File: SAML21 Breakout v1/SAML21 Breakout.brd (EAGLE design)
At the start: 100 x 80 mm, 32 parts, among them J1 M50-4910545, U1 AT-SAM-L21-JTQFP, U2 AP7361C-33E-13, U3 MCP1501-CHY, Y2 32.768MHz

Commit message: dd
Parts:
- moved R3 3.59 mm to (38.1, 17.8), turned to 270 degrees
- moved D2 2.54 mm to (20.3, 17.8), turned to 90 degrees
- moved J1 2.54 mm to (55.9, 66.0)
- moved VREF_EN 2.54 mm to (33.0, 48.3)
- moved C14 1.91 mm to (36.2, 52.1)
- moved U3 1.90 mm to (37.5, 54.6)
- moved R5 1.80 mm to (22.9, 17.8), turned to 270 degrees
- moved D1 1.80 mm to (40.6, 17.8), turned to 90 degrees
- moved R4 1.27 mm to (36.8, 49.5)

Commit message: breakout
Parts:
- added JP1: M142ROWS, dr-library:2X07
- added JP2, JP3, JP8: M122ROWS, dr-library:2X06
- added JP4, JP5, JP6, JP7, JP9: M02LONG, dr-library:1X02-LONG
- moved J1 18.9 mm to (68.6, 52.1)
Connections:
- new net PA0: JP1.1, U1.1
- new net PA1: JP1.2, U1.2
- new net PA10: JP2.3, U1.19
- new net PA11: JP2.4, U1.20
- new net PA12: JP2.11, U1.29
- new net PA13: JP2.12, U1.30
- new net PA16: JP8.1, U1.35
- new net PA17: JP8.2, U1.36
- new net PA18: JP8.3, U1.37
- new net PA19: JP8.4, U1.38
- new net PA2: JP1.3, U1.3
- new net PA20: JP8.7, U1.41
- new net PA21: JP8.8, U1.42
- new net PA22: JP8.9, U1.43
- new net PA23: JP8.10, U1.44
- new net PA24: JP8.11, U1.45
- new net PA25: JP8.12, U1.46
- new net PA27: JP3.3, U1.51
- new net PA4: JP1.11, U1.13
- new net PA5: JP1.12, U1.14
- new net PA6: JP1.13, U1.15
- new net PA7: JP1.14, U1.16
- new net PA8: JP2.1, U1.17
- new net PA9: JP2.2, U1.18
- new net PB0: JP3.9, U1.61
- new net PB1: JP3.10, U1.62
- new net PB10: JP2.5, U1.23
- new net PB11: JP2.6, U1.24
- new net PB12: JP2.7, U1.25
- new net PB13: JP2.8, U1.26
- new net PB14: JP2.9, U1.27
- new net PB15: JP2.10, U1.28
- new net PB16: JP8.5, U1.39
- new net PB17: JP8.6, U1.40
- new net PB2: JP3.11, U1.63
- new net PB22: JP3.1, U1.49
- new net PB23: JP3.2, U1.50
- new net PB3: JP3.12, U1.64
- new net PB30: JP3.7, U1.59
- new net PB31: JP3.8, U1.60
- new net PB4: JP1.5, U1.5
- new net PB5: JP1.6, U1.6
- new net PB6: JP1.7, U1.9
- new net PB7: JP1.8, U1.10
- new net PB8: JP1.9, U1.11
- new net PB9: JP1.10, U1.12
- new net VSW: U1.55
- net +3V3: now also JP5.2, JP6.2, JP7.2, JP9.2
- net GND: now also JP4.2, JP5.1, JP6.1, JP7.1, JP9.1
- net RESET: now also JP3.4
- net SWCLK: now also JP3.5
- net SWDIO: now also JP3.6
- net VCC: now also JP4.1
- net VREF/PA3: now also JP1.4

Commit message: ddx
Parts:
- added D3, D4: PWR, dr-library:LED-1206
- added JP10, JP11: M02, dr-library:1X02
- added Q1, Q2: 2N7002, dr-library:SOT-23-3
- added R6, R8: 330, dr-library:RES-0603
- added R7, R9: 10k, dr-library:RES-0603
- added U$2, U$3, U$4, U$5: (no value), EmbeddedAdventures 3:STAND-OFF-HOLE
- moved JP4 80.3 mm to (94.0, 11.4), turned to 180 degrees
- moved D2 73.7 mm to (94.0, 17.8), turned to 180 degrees
- moved R5 71.2 mm to (94.0, 20.3), turned to 0 degrees
- moved C12 68.2 mm to (94.0, 23.5), turned to 180 degrees
- moved U2 64.3 mm to (94.0, 27.9), turned to 90 degrees
- moved C13 60.8 mm to (94.0, 32.4), turned to 180 degrees
- moved R3 58.6 mm to (94.0, 35.6), turned to 0 degrees
- moved D1 57.1 mm to (94.0, 38.1), turned to 180 degrees
- moved JP5 55.1 mm to (94.0, 41.9), turned to 0 degrees
- moved JP2 39.0 mm to (16.5, 11.4)
- moved JP6 37.8 mm to (11.4, 10.2)
- moved JP3 25.4 mm to (39.4, 59.7)
- moved JP7 25.4 mm to (22.9, 61.0)
- moved C3 19.2 mm to (36.8, 48.9)
- moved C5 19.2 mm to (46.4, 34.3)
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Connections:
- new net HEART: JP10.2, Q1.D, R7.1
- new net HEART2: JP11.2, Q2.D, R9.1
- new net N$10: D4.A, R8.1
- new net N$11: D4.C, Q2.G
- new net N$8: D3.A, R6.1
- new net N$9: D3.C, Q1.G
- net +3V3: now also R6.2, R8.2
- net GND: now also Q1.S, Q2.S, R7.2, R9.2
- net PA8: now also JP10.1
- net PB10: now also JP11.1
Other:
- board size 100 x 80 mm -> 76.2 x 63.5 mm

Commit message: component layout
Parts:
- added D5: VS-10BQ030-M3, dr-library:DO-214AA
- added J2: (no value), EmbeddedAdventures 3:SPC4077
- moved JP5 56.8 mm to (50.8, 5.08), turned to 90 degrees
- moved J1 54.6 mm to (7.62, 50.8)
- moved C12 52.6 mm to (46.4, 45.7), turned to 0 degrees
- moved U2 49.5 mm to (46.4, 41.3), turned to 270 degrees
- moved C13 47.8 mm to (46.4, 36.8), turned to 0 degrees
- moved S1 46.7 mm to (36.8, 58.4), turned to 180 degrees
- moved R2 43.5 mm to (43.2, 58.4), turned to 270 degrees
- moved R5 43.0 mm to (53.3, 34.3), turned to 180 degrees
- moved R8 41.6 mm to (53.3, 26.7), turned to 180 degrees
- moved R3 40.8 mm to (53.3, 31.8), turned to 180 degrees
- moved C9 39.8 mm to (36.8, 54.6), turned to 0 degrees
- moved D2 39.2 mm to (58.4, 34.3), turned to 0 degrees
- moved JP11 38.6 mm to (45.7, 31.8)
- moved R9 37.7 mm to (54.0, 21.6)
- moved JP10 37.4 mm to (45.7, 26.7)
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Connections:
- new net N$12: D5.A, J2.3
- net +3V3: no longer JP9.2
- net GND: now also J2.2, JP9.2; no longer JP9.1
- net VCC: now also D5.C, JP9.1
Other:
- board size 76.2 x 63.5 mm -> 63.5 x 63.5 mm

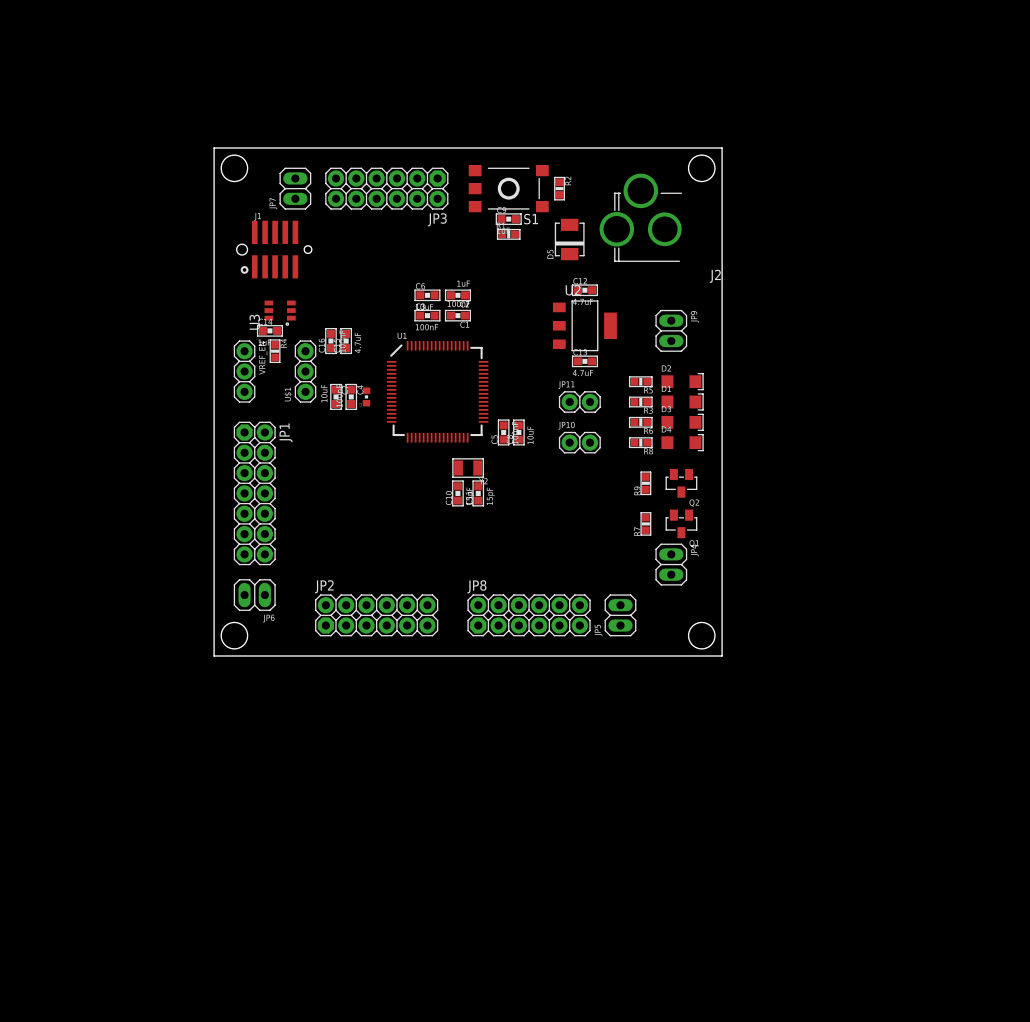
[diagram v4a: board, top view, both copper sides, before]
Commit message: Added USB interface
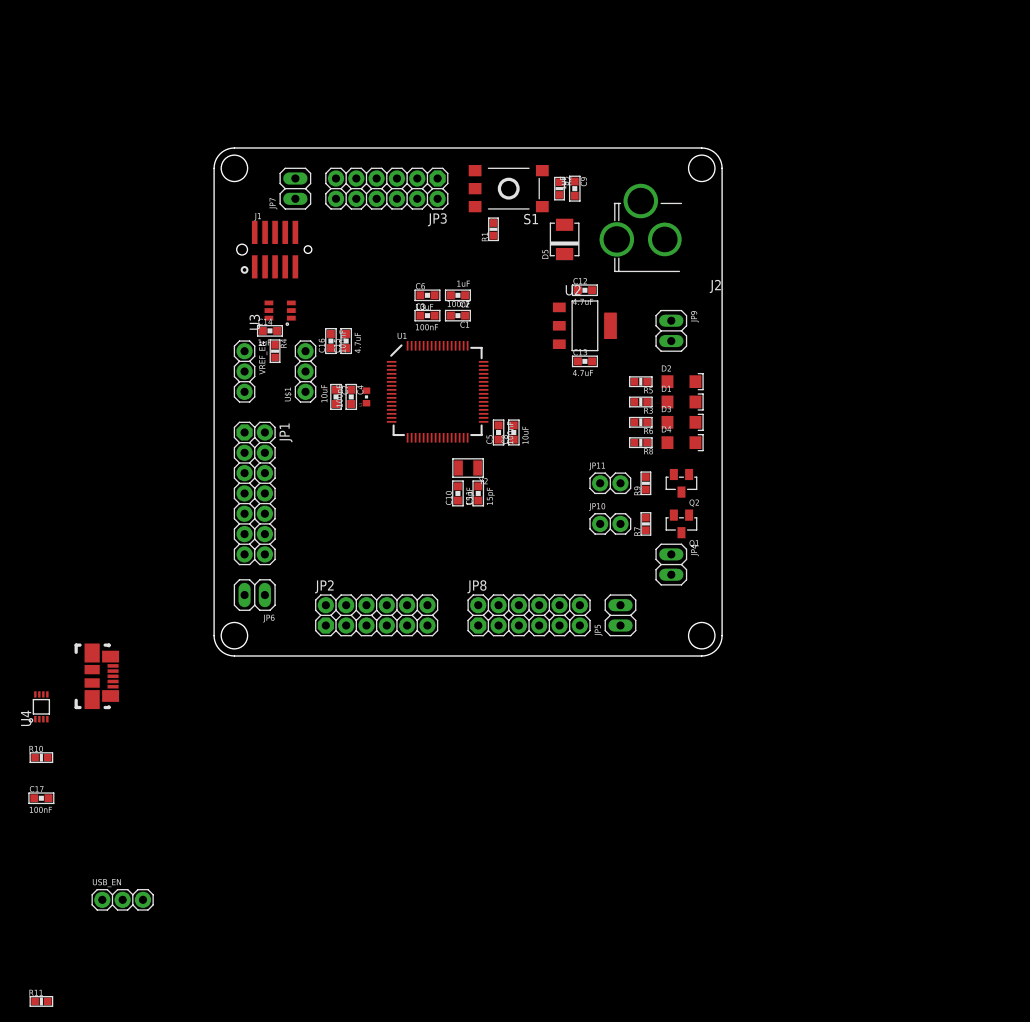
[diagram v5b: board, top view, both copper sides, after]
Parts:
- added C17: 100nF, dr-library:CAP-0603
- added R10, R11: 10k, dr-library:RES-0603
- added U$6: MOLEX_USBMICRO, dr-library:MOLEX_47346-001
- added U4: TXS-0102-Q1, dr-library:VSSOP-8
- added USB_EN: M03, dr-library:1X03
- moved JP10 10.9 mm to (49.5, 16.5)
- moved JP11 10.9 mm to (49.5, 21.6)
- moved C9 9.09 mm to (45.1, 58.4), turned to 270 degrees
- moved R1 2.01 mm to (34.9, 53.3), turned to 90 degrees
- moved J2 1.27 mm to (53.3, 52.1)
- moved D5 0.64 mm to (43.8, 52.1)
- moved C5 0.63 mm to (35.6, 27.9)
- moved C8 0.63 mm to (37.5, 27.9)
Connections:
- removed net PA24: JP8.11, U1.45
- removed net PA25: JP8.12, U1.46
- new net N$13: R10.1, USB_EN.1
- new net N$14: U$6.2, U4.8
- new net N$15: U$6.3, U4.1
- new net N$17: R11.2, USB_EN.3
- new net N$19: U4.6, USB_EN.2
- new net PA24/D-: JP8.11, U1.45, U4.5
- new net PA25/D+: JP8.12, U1.46, U4.4
- net +3V3: now also R10.2, U4.3
- net GND: now also C17.2, R11.1, U$6.5, U4.2
- net VCC: now also C17.1, U$6.1, U4.7
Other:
- outline, holes or cut-outs redrawn

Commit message: pcb layout
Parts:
- removed U2: AP7361C-33E-13, dr-library:SOT-223-3
- added U5: AP7362-33SP-13, dr-library:SO-8EP
- C12, C13: value 4.7uF -> 10uF
- moved R11 105.0 mm to (38.1, 43.2)
- moved C17 101.0 mm to (55.9, 47.0), turned to 270 degrees
- moved USB_EN 93.7 mm to (41.9, 45.7), turned to 180 degrees
- moved U$6 93.0 mm to (61.0, 50.8), turned to 180 degrees
- moved U4 87.1 mm to (48.3, 45.7), turned to 270 degrees
- moved R10 85.5 mm to (43.2, 43.2)
- moved C13 18.3 mm to (41.9, 54.6), turned to 270 degrees
- moved R4 12.9 mm to (3.17, 50.2)
- moved C9 12.7 mm to (45.1, 71.1)
- moved R1 12.7 mm to (34.9, 66.0), turned to 270 degrees
- moved R2 12.7 mm to (43.2, 71.1)
- moved S1 12.7 mm to (36.8, 71.1)
- moved D5 12.7 mm to (43.8, 64.8)
- moved J2 12.7 mm to (53.3, 64.8)
- moved U$3 12.7 mm to (2.54, 73.7)
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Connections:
- net +3V3: now also U5.5, U5.6, U5.7; no longer U2.3
- net GND: now also U5.1, U5.PAD; no longer U2.2
- net PA3: now also JP1.4
- net VCC: now also U5.2, U5.3, U5.4; no longer U2.1
- net VREF/PA3: no longer JP1.4
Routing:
- net +3V3: track 0.00 -> 359.7 mm, vias 0 -> 12
- net GND: track 0.00 -> 144.6 mm, vias 0 -> 9
- net VCC: track 0.00 -> 86.7 mm, vias 0 -> 2
- net RESET: track 0.00 -> 80.0 mm, vias 0 -> 2
- net PA8: track 0.00 -> 78.9 mm
- net PB10: track 0.00 -> 76.2 mm
- net PA24/D-: track 0.00 -> 58.5 mm, vias 0 -> 1
- net SWCLK: track 0.00 -> 57.6 mm, vias 0 -> 1
- net PA25/D+: track 0.00 -> 51.6 mm, vias 0 -> 1
- net SWDIO: track 0.00 -> 51.5 mm, vias 0 -> 1
- net PA22: track 0.00 -> 43.9 mm
- net PA20: track 0.00 -> 42.0 mm
- net PA23: track 0.00 -> 41.7 mm
- net PB16: track 0.00 -> 40.1 mm
- net PA21: track 0.00 -> 39.8 mm
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- added copper zone on layer 1, net +3V3
- added copper zone on layer 16, net +3V3
- added copper zone on layer 1, net GND
- added copper zone on layer 16, net GND
- added copper zone on layer 1, net N$3
- added copper zone on layer 1, net VCC
- added copper zone on layer 16, net VCC
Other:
- board size 63.5 x 63.5 mm -> 63.5 x 76.2 mm
- board text added: "3V3"
- board text added: "GND"
- board text added: "PA0"
- board text added: "PA1"
- board text added: "PA10"
- board text added: "PA11"
- board text added: "PA12"
- board text added: "PA13"
- board text added: "PA16"
- board text added: "PA17"
- board text added: "PA18"
- board text added: "PA19"
- board text added: "PA2"
- board text added: "PA21"
- board text added: "PA22"
- board text added: "PA23"
- board text added: "PA24"
- board text added: "PA25"
- board text added: "PA27"
- board text added: "PA3"
- board text added: "PA30"
- board text added: "PA31"
- board text added: "PA4"
- board text added: "PA5"
- board text added: "PA6"
- board text added: "PA7"
- board text added: "PA8"
- board text added: "PA9"
- board text added: "PB0"
- board text added: "PB1"
- board text added: "PB10"
- board text added: "PB11"
- board text added: "PB12"
- board text added: "PB13"
- board text added: "PB14"
- board text added: "PB15"
- board text added: "PB16"
- board text added: "PB17"
- board text added: "PB2"
- board text added: "PB20"
- board text added: "PB22"
- board text added: "PB23"
- board text added: "PB3"
- board text added: "PB30"
- board text added: "PB31"
- board text added: "PB4"
- board text added: "PB5"
- board text added: "PB6"
- board text added: "PB7"
- board text added: "PB8"
- board text added: "PB9"
- board text added: "RST"
- board text added: "VCC"
- board text added: "VREF_SEL"

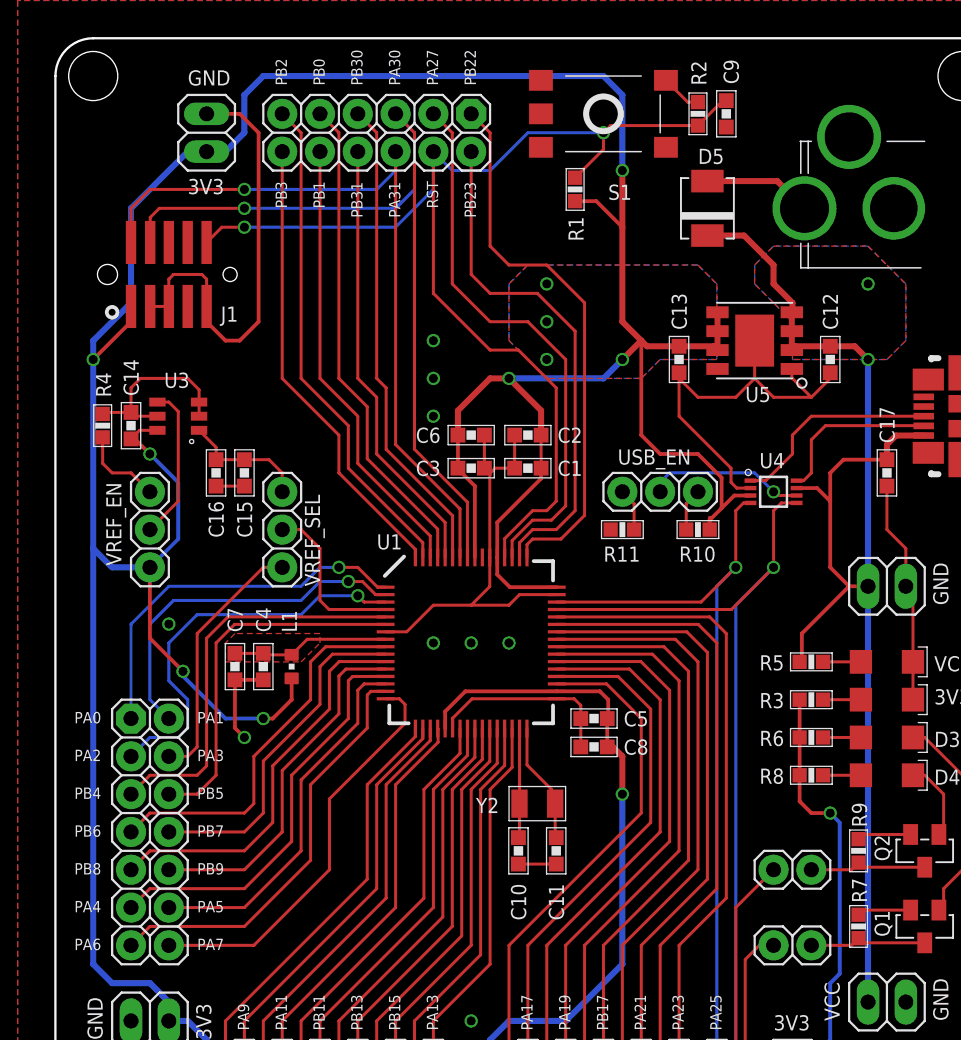
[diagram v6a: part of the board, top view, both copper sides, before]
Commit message: Component size change
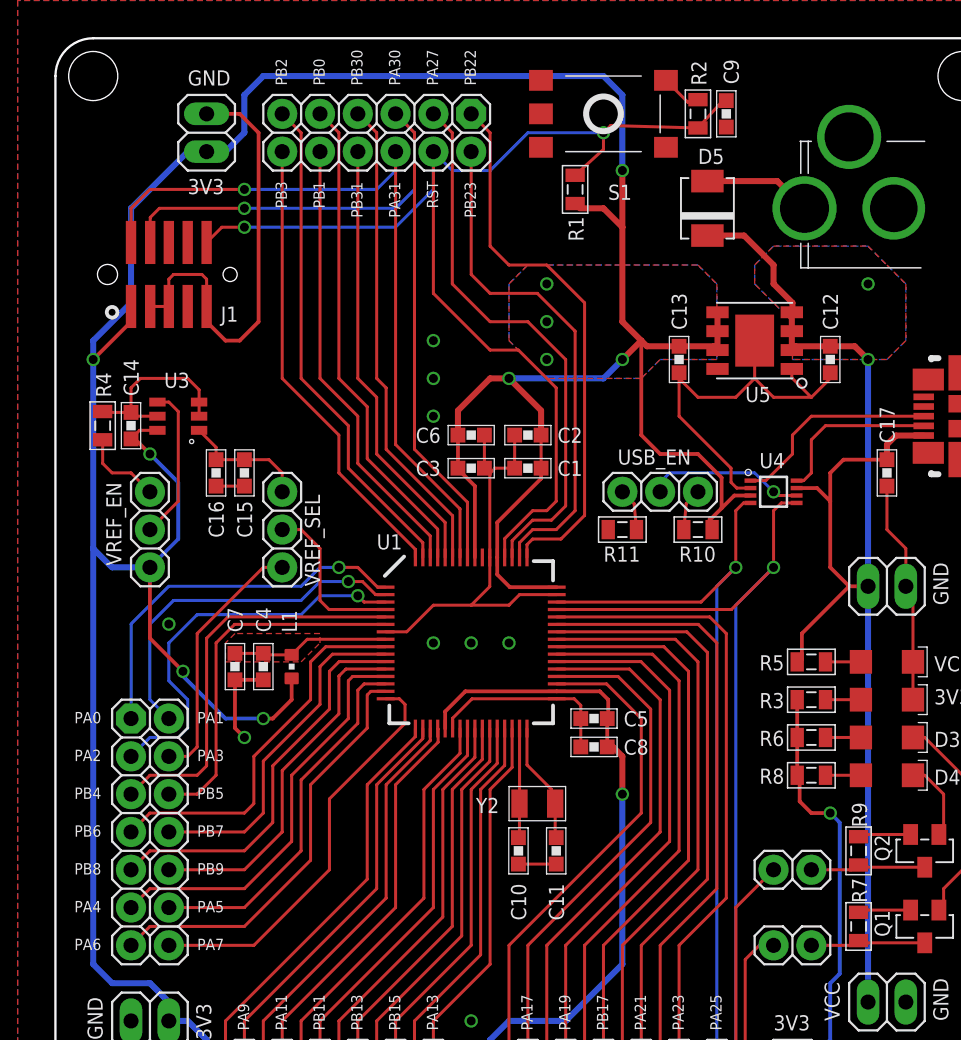
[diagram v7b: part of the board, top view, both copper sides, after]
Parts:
- R1, R10, R11, R2, R3, R4, R5, R6, R7, R8, R9: device dr-library:RES-0603 -> dr-library:RES-0805
